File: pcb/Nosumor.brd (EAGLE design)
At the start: 50 x 50 mm, 126 parts, among them IC1 STM32F722RET, J4 SJ-43515TS-SMT-EDGE, J5 CX90M-16P, J6 CX90M-16P, K1 CHERRY-MX, K2 CHERRY-MX, K3 KSC623J, K4 KSC623J, K5 KSC623J, Q1 ABM8W-12.0000MHZ, Q2 CX2016DB, Q3 FDY100PZ, Q4 FDY100PZ, Q5 FDY100PZ, Q6 FDY100PZ, U1 3.3V, U2 FT2232H-56Q-REEL, U3 3.3V, U4 24CW1280T-I/OT, U5 9DoF IMU, U6 3.3V, U7 USB3370, U8 TLV320AIC3256

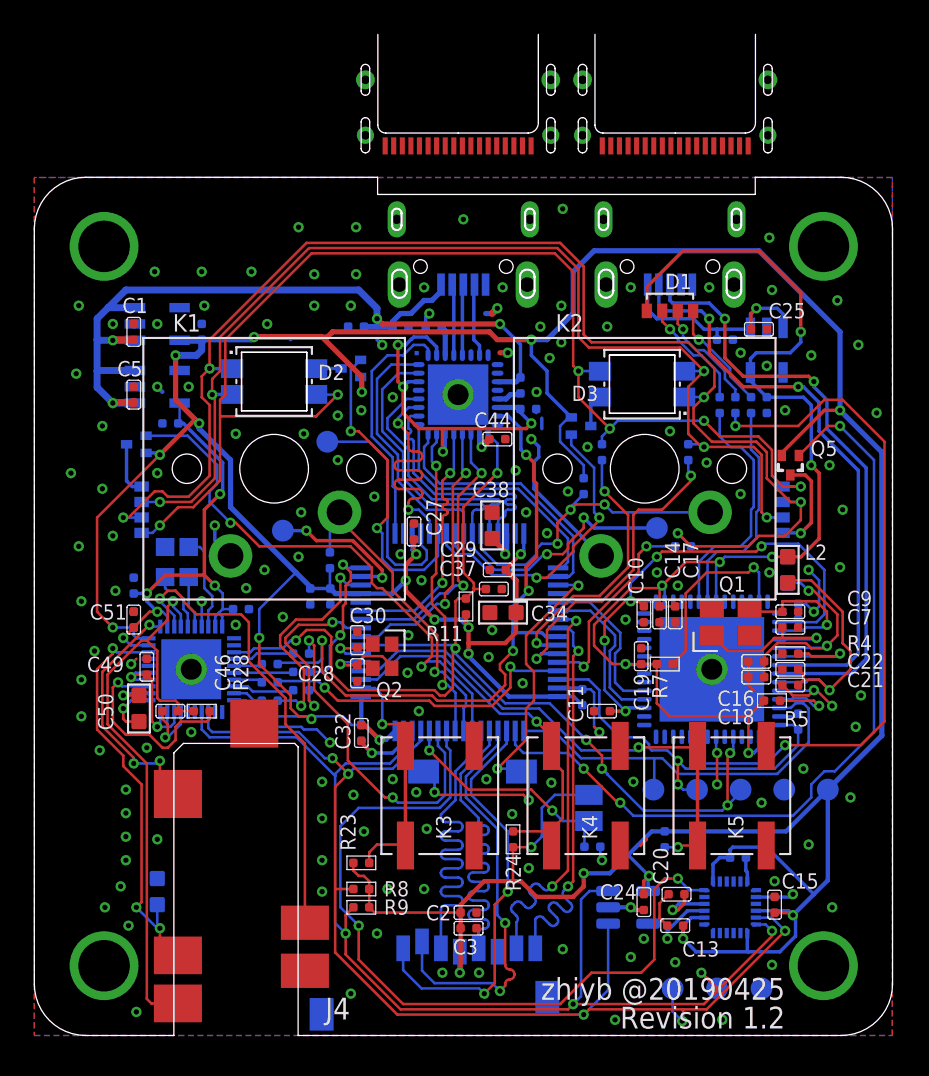
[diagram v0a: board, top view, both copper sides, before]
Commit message: PCB revision 1.3 with USB Type-C, more datasheets
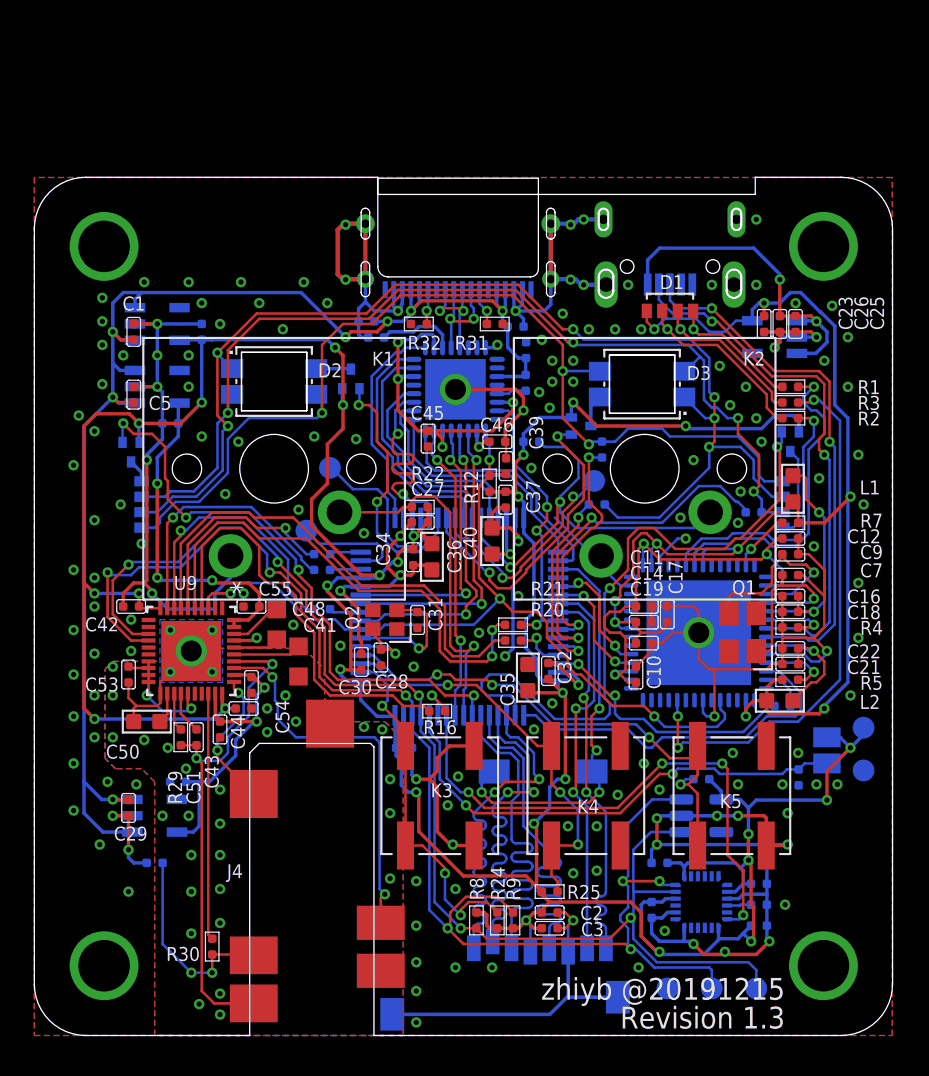
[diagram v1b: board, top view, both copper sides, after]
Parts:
- removed J5, J6: CX90M-16P, connector:CX90M-16P
- removed L3: 120OHM-500MA, Seeed-Inductor:L0603
- removed TP11, TP3, TP7: TPB1,27, testpad:B1,27
- added C53, C54, C55: 100nf, Seeed-Capacitor:C0402
- added R29: 2k7, Seeed-Resistor:R0402
- added R30: 0, Seeed-Resistor:R0402
- added R31, R32: 5k1, Seeed-Resistor:R0402
- added U9: TLV320AIC3256, ti:QFN40P500X500X80-41N
- C29: value 100n -> 4u7
- C30: value 12pf -> 100n
- C31: value 100n -> 12pf
- C34: value 4u7 -> 100n; device Seeed-Capacitor:C0603 -> Seeed-Capacitor:C0402
- C35: device Seeed-Capacitor:C0402 -> Seeed-Capacitor:C0603
- C36: value 100n -> 4u7; device Seeed-Capacitor:C0402 -> Seeed-Capacitor:C0603
- C38: device Seeed-Capacitor:C0603 -> Seeed-Capacitor:C0402
- C39: value 2u2 -> 100n; device rcl:C0603K -> Seeed-Capacitor:C0402
- C40: value 100nf -> 4u7; device Seeed-Capacitor:C0402 -> Seeed-Capacitor:C0603
- C41, C48: value 100nf -> 2u2; device Seeed-Capacitor:C0402 -> rcl:C0603K
- C43, C44: value 4u7 -> 100nf
- C46: value 100nf -> 4u7
- C47: value 2u2 -> 4u7; device rcl:C0603K -> Seeed-Capacitor:C0402
- J3: value (none) -> CX90M-16P; device Wurth_Elektronik_Electromechanic_Input-Output_Connectors_rev16b:629105150521 -> connector:CX90M-16P
- R11: value 10K 1/16W -> 0
- R12: value 100R -> 10K 1/16W
- R15: value 27R -> 100R
- R20: value 10R -> 27R
- R21: value 10K 1/16W -> 10R
- R27: value 20K -> 10K 1/16W
- R28: value 2k7 -> 20K
- U3: value 3.3V -> 1.8V
- U7: value USB3370 -> 1.8V; device microchip:QFN32 -> SparkFun-IC-Power:SOT23-5
- U8: value TLV320AIC3256 -> USB3370; device ti:QFN40P500X500X80-41N -> microchip:QFN32
- moved R26 30.6 mm to (38.9, 14.9)
- moved U7 30.2 mm to (7.01, 12.8), turned to 90 degrees
- moved C49 28.8 mm to (28.7, 39.9), flipped to the bottom, turned to 0 degrees
- moved C52 26.9 mm to (28.0, 41.3), turned to 90 degrees
- moved R28 26.9 mm to (28.6, 38.0), flipped to the bottom, turned to 180 degrees
- moved R23 26.5 mm to (29.0, 34.6), flipped to the bottom, turned to 90 degrees
- moved C43 25.9 mm to (10.8, 17.8), flipped to the top, turned to 180 degrees
- moved C29 25.6 mm to (5.49, 13.3), turned to 180 degrees
- moved C46 24.7 mm to (27.0, 34.6), turned to 270 degrees
- moved C38 23.6 mm to (8.38, 14.8), flipped to the bottom, turned to 270 degrees
- moved R11 23.5 mm to (7.01, 10.1), flipped to the bottom, turned to 270 degrees
- moved U8 22.4 mm to (24.5, 37.6), turned to 270 degrees
- moved C44 21.6 mm to (12.2, 19.1)
- moved C40 21.4 mm to (26.7, 28.8), flipped to the top
- moved C39 20.6 mm to (27.5, 33.2), flipped to the top, turned to 0 degrees
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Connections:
- net N$43 renamed DBG_DP
- net N$51 renamed DBG_DM
- removed net N$14: J4.4, L3.1, U8.28
- removed net N$2: R16.2, U8.8
- removed net N$22: R17.2, U8.6
- removed net N$3: R18.2, U8.9
- removed net N$33: C43.2, U7.14, U7.2, U7.22, U7.30
- removed net N$36: C44.2, U7.18
- removed net N$40: R20.2, U8.5
- removed net N$7: R15.2, U8.4
- new net AGND: C38.1, C41.2, C43.1, C44.1, C50.2, C53.2, C54.2, J4.4, R11.2, R30.2, U9.21, U9.41
- new net AIC_BCLK_R: R18.2, U9.6
- new net AIC_DIN_R: R17.2, U9.8
- new net AIC_DOUT_R: R19.2, U9.9
- new net AIC_GPIO_R: R16.2, U9.4
- new net AIC_MCLK_R: R21.2, U9.5
- new net AIC_WCLK_R: R20.2, U9.7
- new net AVDD: C38.2, C43.2, C54.1, U7.5, U9.29, U9.32
- new net N$10: C51.1, U9.24
- new net VUSB18: C46.2, U8.18
- new net VUSB33: C45.2, U8.14, U8.2, U8.22, U8.30
- net +1V8: now also C55.1, U9.39, U9.40; no longer C41.2, C51.1, C52.1, U8.29, U8.32, U8.39, U8.40
- net +3V3: now also C30.2, C37.2, C44.2, R12.2, R26.2, U9.10, U9.30; no longer C29.2, C31.2, C40.2, R11.2, R21.2, U8.10, U8.30
- net +5V: now also C29.2, C47.2, C49.2, C52.2, J3.A4, J3.A9, J3.B4, J3.B9, R28.2, U7.1, U7.3, U8.11; no longer C45.2, C48.2, J3.1, R27.2, U7.11
- net AIC_BCLK: now also R18.1; no longer R17.1
- net AIC_DIN: now also R17.1; no longer R16.1
- net AIC_DOUT: now also R19.1; no longer R18.1
- net AIC_GPIO: now also R16.1; no longer R15.1
- net AIC_WCLK: now also R20.1; no longer R19.1
- net GND: now also C39.1, C46.1, C47.1, C49.1, C52.1, C55.2, J3.A1, J3.A12, J3.B1, J3.B12, R11.1, R27.1, R31.1, R32.1, U7.2, U8.8, U8.EXP, U9.1, U9.11, U9.16, U9.2, U9.37; no longer C38.1, C39.2, C41.1, C43.1, C44.1, C48.1, C49.2, C50.2, C51.2, C52.2, J3.5, L3.2, R26.1, U7.8, U7.EXP, U8.1, U8.11, U8.16, U8.2, U8.21, U8.37, U8.41
- net I2C_SCL: now also U9.13; no longer U8.13
- net I2C_SDA: now also U9.14; no longer U8.14
- net KEY_1: now also R22.1; no longer R21.1
- net KEY_2: now also R23.1; no longer R22.1
- net KEY_3: now also R24.1; no longer R23.1
- net KEY_4: now also R25.1; no longer R24.1
- net KEY_5: now also R26.1; no longer R25.1
- net LED_B: now also R15.1; no longer R14.1
- net LED_G: now also R14.1; no longer R13.1
- net LED_R: now also R13.1; no longer R12.1
- net MCLK: now also R21.1, U8.15; no longer R20.1, U7.15
- net N$1: now also J3.A5, R32.2; no longer R19.2, U8.7
- net N$12: now also U9.33; no longer U8.33
- net N$13: now also U9.31; no longer U8.31
- net N$17: now also C51.2, R29.2, U9.34; no longer C46.2, R28.2, U8.34
- net N$18: now also R29.1, U9.23; no longer R28.1, U8.23
- net N$19: now also R30.1, U9.28; no longer C46.1, U8.17
- net N$20: now also C53.1, U9.17, U9.18, U9.19, U9.20, U9.25; no longer C49.1, U8.18, U8.19, U8.20, U8.24, U8.25
- net N$21: now also U9.22; no longer U8.22
- net N$23: now also C48.1, U9.36; no longer C47.1, U8.36
- net N$25: now also C48.2, U9.38; no longer C47.2, U8.38
- net N$26: now also C31.2; no longer C30.2
- net N$29: now also C40.2; no longer C38.2
- net N$32: now also R28.1, U8.13; no longer R27.1, U7.13
- net N$37: now also R27.2, U8.3; no longer R26.2, U7.3
- net N$38: now also C41.1, U9.35; no longer C39.1, U8.35
- net N$4: now also J3.A7, J3.B7, U8.4; no longer J3.2, U7.4
- net N$5: now also J3.A6, J3.B6, U8.5; no longer J3.3, U7.5
- net N$6: now also J3.B5, R31.2; no longer J3.4, U7.7
- net RGB_B: now also R15.2; no longer R14.2
- net RGB_G: now also R14.2; no longer R13.2
- net RGB_R: now also R13.2; no longer R12.2
- net SRST_N: now also C39.2, R12.1, U8.17, U9.3; no longer C37.2, R11.1, TP11.TP, U7.17, U8.3
- net SWCLK: no longer TP3.TP
- net SWDIO: no longer TP7.TP
- net ULPI_CLK: now also U8.27; no longer U7.27
- net ULPI_D0: now also U8.1; no longer U7.1
- net ULPI_D1: now also U8.32; no longer U7.32
- net ULPI_D2: now also U8.31; no longer U7.31
- net ULPI_D3: now also U8.28; no longer U7.28
- net ULPI_D4: now also U8.26; no longer U7.26
- net ULPI_D5: now also U8.25; no longer U7.25
- net ULPI_D6: now also U8.24; no longer U7.24
- net ULPI_D7: now also U8.23; no longer U7.23
- net ULPI_DIR: now also U8.19; no longer U7.19
- net ULPI_NXT: now also U8.21; no longer U7.21
- net ULPI_STP: now also U8.20; no longer U7.20
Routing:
- net GND: track 64.3 -> 254.4 mm, vias 161 -> 164
- net +3V3: track 279.8 -> 226.3 mm, vias 23 -> 28
- net +5V: track 51.8 -> 83.6 mm, vias 4 -> 7
- net AIC_MCLK_R: track 0.00 -> 28.8 mm, vias 0 -> 2
- net AIC_WCLK_R: track 0.00 -> 28.7 mm
- net AIC_GPIO_R: track 0.00 -> 24.9 mm
- net N$14: track 24.2 -> 0.00 mm, vias 3 -> 0
- net MCLK: track 38.2 -> 16.8 mm, vias 4 -> 3
- net N$33: track 21.1 -> 0.00 mm, vias 4 -> 0
- net AGND: track 0.00 -> 19.6 mm, vias 0 -> 35
- net VUSB33: track 0.00 -> 19.1 mm, vias 0 -> 4
- net AVDD: track 0.00 -> 18.2 mm, vias 0 -> 2
- net AIC_GPIO: track 19.5 -> 2.53 mm, vias 2 -> 1
- net AIC_DIN_R: track 0.00 -> 16.0 mm, vias 0 -> 1
- net AIC_WCLK: track 18.7 -> 3.00 mm, vias 2 -> 1
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- added copper zone on layer 1, net AGND
- added copper zone on layer 16, net AGND
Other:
- outline, holes or cut-outs redrawn
- board text added: "Revision 1.3"
- board text added: "zhiyb @20191215"
- board text removed: "R"
- board text removed: "Revision 1.2"
- board text removed: "zhiyb @20190425"
